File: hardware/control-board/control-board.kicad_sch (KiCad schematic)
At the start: 28 parts, among them J1 JACK_2P, J12 JACK_2P, J14 Top Left(M), J16 Top Right (M), J18 Bottom Left(M), J2 JACK_2P, J20 Bottom Right(M), J3 JACK_2P, J4 JACK_2P, J5 JACK_2P, J6 JACK_2P, J7 JACK_2P, J8 JACK_2P

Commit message: chore: restructure project
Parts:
- J1, J12, J2, J3, J4, J5, J6, J7, J8: symbol cem-3340:AudioJack2_SwitchT -> Eurorack Common:AudioJack2_SwitchT
- RV3, RV4, RV5: footprint cem-3340:Alpha Potentiometer -> Eurorack Common:Alpha Potentiometer
- S1: footprint cem-3340:Sub-Miniature SPDT -> Eurorack Common:Sub-Miniature SPDT
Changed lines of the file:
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@@
 	)
 	(symbol
-		(lib_id "cem-3340:AudioJack2_SwitchT")
+		(lib_id "Eurorack Common:AudioJack2_SwitchT")
 		(at 35.56 139.7 0)
 		(unit 1)
@@
 	)
 	(symbol
-		(lib_id "cem-3340:AudioJack2_SwitchT")
+		(lib_id "Eurorack Common:AudioJack2_SwitchT")
 		(at 234.95 121.92 180)
 		(unit 1)
@@
 	)
 	(symbol
-		(lib_id "cem-3340:AudioJack2_SwitchT")
+		(lib_id "Eurorack Common:AudioJack2_SwitchT")
 		(at 35.56 162.56 0)
 		(unit 1)
@@
 			)
 		)
-		(property "Footprint" "cem-3340:Sub-Miniature SPDT"
+		(property "Footprint" "Eurorack Common:Sub-Miniature SPDT"
 			(at 60.96 139.7 0)
 			(effects
@@
 	)
 	(symbol
-		(lib_id "cem-3340:AudioJack2_SwitchT")
+		(lib_id "Eurorack Common:AudioJack2_SwitchT")
 		(at 236.22 74.93 180)
 		(unit 1)
@@
 	)
 	(symbol
-		(lib_id "cem-3340:AudioJack2_SwitchT")
+		(lib_id "Eurorack Common:AudioJack2_SwitchT")
 		(at 234.95 99.06 180)
 		(unit 1)
@@
 			)
 		)
-		(property "Footprint" "cem-3340:Alpha Potentiometer"
+		(property "Footprint" "Eurorack Common:Alpha Potentiometer"
 			(at 50.8 116.84 0)
 			(effects
@@
 			)
 		)
-		(property "Footprint" "cem-3340:Alpha Potentiometer"
+		(property "Footprint" "Eurorack Common:Alpha Potentiometer"
 			(at 43.18 41.91 0)
 			(effects
@@
 	)
 	(symbol
-		(lib_id "cem-3340:AudioJack2_SwitchT")
+		(lib_id "Eurorack Common:AudioJack2_SwitchT")
 		(at 35.56 120.65 0)
 		(unit 1)
@@
 	)
 	(symbol
-		(lib_id "cem-3340:AudioJack2_SwitchT")
+		(lib_id "Eurorack Common:AudioJack2_SwitchT")
 		(at 234.95 144.78 180)
 		(unit 1)
@@
 	)
 	(symbol
-		(lib_id "cem-3340:AudioJack2_SwitchT")
+		(lib_id "Eurorack Common:AudioJack2_SwitchT")
 		(at 35.56 93.98 0)
 		(unit 1)
@@
 	)
 	(symbol
-		(lib_id "cem-3340:AudioJack2_SwitchT")
+		(lib_id "Eurorack Common:AudioJack2_SwitchT")
 		(at 35.56 78.74 0)
 		(unit 1)
@@
 			)
 		)
-		(property "Footprint" "cem-3340:Alpha Potentiometer"
+		(property "Footprint" "Eurorack Common:Alpha Potentiometer"
 			(at 43.18 60.96 0)
 			(effects

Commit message: feature: docs
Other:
- title: (none) -> CEM3340 VCO - Control Board
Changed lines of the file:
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@@
 	(generator_version "9.0")
 	(paper "A4")
+	(title_block
+		(title "CEM3340 VCO - Control Board")
+		(date "2025-11-05")
+		(rev "v1.0.0")
+	)
 	(text "Frequency"
 		(exclude_from_sim no)

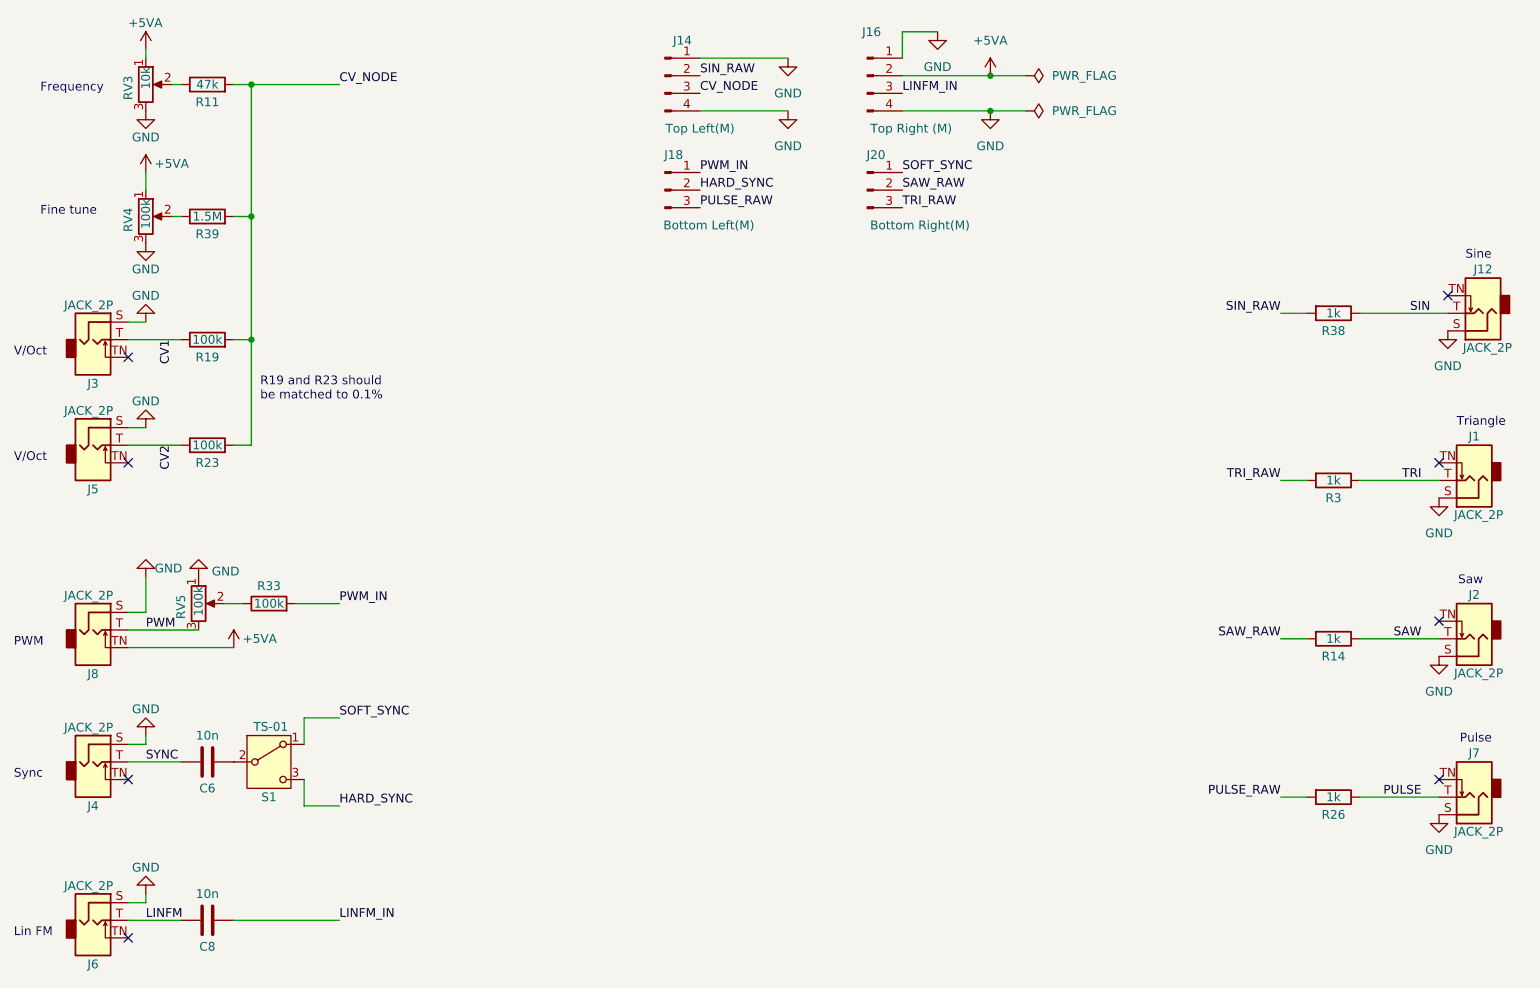
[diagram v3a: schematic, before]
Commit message: feature: improve docs + front panel design
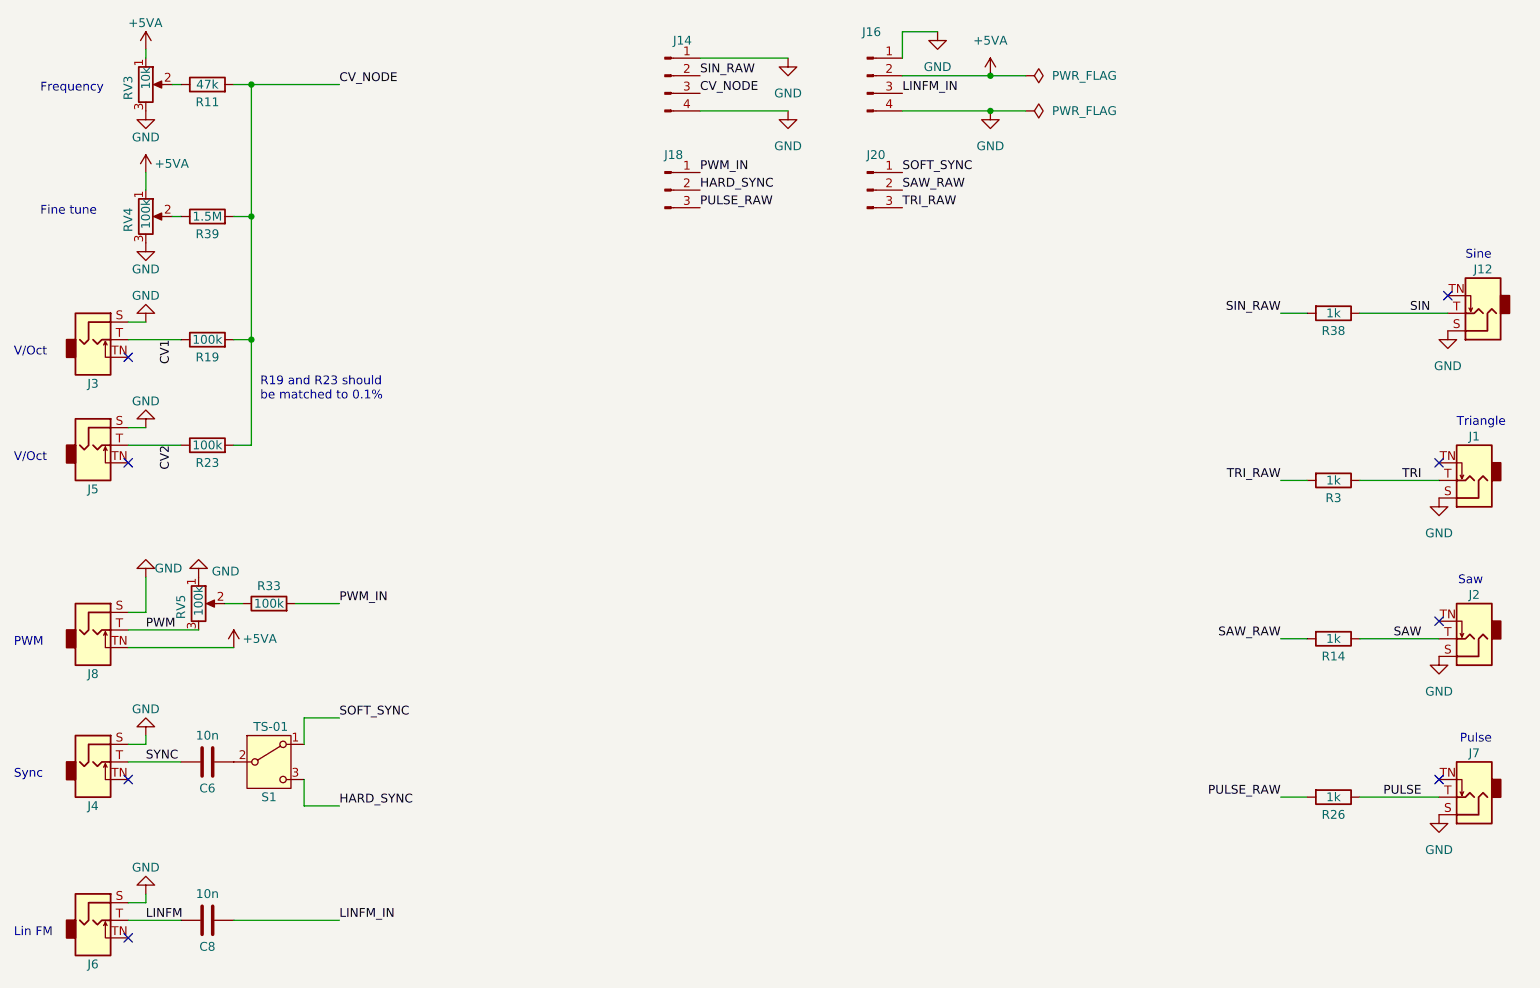
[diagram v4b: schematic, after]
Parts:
- C6, C8: footprint Capacitor_THT:C_Rect_L4.6mm_W3.0mm_P2.50mm_MKS02_FKP02 -> Eurorack Common:C_Disc_D3.4mm_W2.1mm_P2.50mm; Note (none) -> X7R ceramic, 2.5mm pitch; Reference_Part (none) -> C322C103K1R5TA; Tolerance (none) -> 10%
- J1, J12, J2, J3, J4, J5, J6, J7, J8: value JACK_2P -> ~; footprint Connector_Audio:Jack_3.5mm_QingPu_WQP-PJ398SM_Vertical_CircularHoles -> Eurorack Common:Thonkicon; Reference_Part (none) -> Thonkiconn
- J14: value Top Left(M) -> ~; footprint Connector_PinHeader_2.54mm:PinHeader_1x04_P2.54mm_Vertical -> Eurorack Common:PinHeader_1x04_P2.54mm_Vertical; Reference_Part (none) -> 1x4 pin header
- J16: value Top Right (M) -> ~; footprint Connector_PinHeader_2.54mm:PinHeader_1x04_P2.54mm_Vertical -> Eurorack Common:PinHeader_1x04_P2.54mm_Vertical; Reference_Part (none) -> 1x4 pin header
- J18: value Bottom Left(M) -> ~; footprint Connector_PinHeader_2.54mm:PinHeader_1x03_P2.54mm_Vertical -> Eurorack Common:PinHeader_1x03_P2.54mm_Vertical; Reference_Part (none) -> 1x3 pin header
- J20: value Bottom Right(M) -> ~; footprint Connector_PinHeader_2.54mm:PinHeader_1x03_P2.54mm_Vertical -> Eurorack Common:PinHeader_1x03_P2.54mm_Vertical; Reference_Part (none) -> 1x3 pin header
- R11: footprint Resistor_THT:R_Axial_DIN0207_L6.3mm_D2.5mm_P7.62mm_Horizontal -> Eurorack Common:R_Axial_DIN0207_L6.3mm_D2.5mm_P7.62mm_Horizontal; Reference_Part (none) -> MF1/4DC4702F; Tolerance (none) -> 1%
- R14, R26, R3, R38: footprint Resistor_THT:R_Axial_DIN0207_L6.3mm_D2.5mm_P7.62mm_Horizontal -> Eurorack Common:R_Axial_DIN0207_L6.3mm_D2.5mm_P7.62mm_Horizontal; Reference_Part (none) -> MF1/4DC1001F; Tolerance (none) -> 1%
- R19, R23: footprint Resistor_THT:R_Axial_DIN0207_L6.3mm_D2.5mm_P7.62mm_Horizontal -> Eurorack Common:R_Axial_DIN0207_L6.3mm_D2.5mm_P7.62mm_Horizontal; Note (none) -> Matched to 0.1% (within 100 ohms); Reference_Part (none) -> MF1/4DC1003F; Tolerance (none) -> 1%
- R33: footprint Resistor_THT:R_Axial_DIN0207_L6.3mm_D2.5mm_P7.62mm_Horizontal -> Eurorack Common:R_Axial_DIN0207_L6.3mm_D2.5mm_P7.62mm_Horizontal; Reference_Part (none) -> MF1/4DC1003F; Tolerance (none) -> 1%
- R39: footprint Resistor_THT:R_Axial_DIN0207_L6.3mm_D2.5mm_P7.62mm_Horizontal -> Eurorack Common:R_Axial_DIN0207_L6.3mm_D2.5mm_P7.62mm_Horizontal; Reference_Part (none) -> MF1/4DC1504F; Tolerance (none) -> 1%
- RV3: Note (none) -> Alpha 9mm vertical, metal shaft; Reference_Part (none) -> RD901F-40-15R1-B10K
- RV4, RV5: Note (none) -> Alpha 9mm vertical, metal shaft; Reference_Part (none) -> RD901F-40-15R1-B100K
- S1: Note (none) -> Sub-miniature ON-ON SPDT; Reference_Part (none) -> 2MS1T1B1M2QES-5
